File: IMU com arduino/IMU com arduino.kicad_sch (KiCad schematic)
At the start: 2 parts

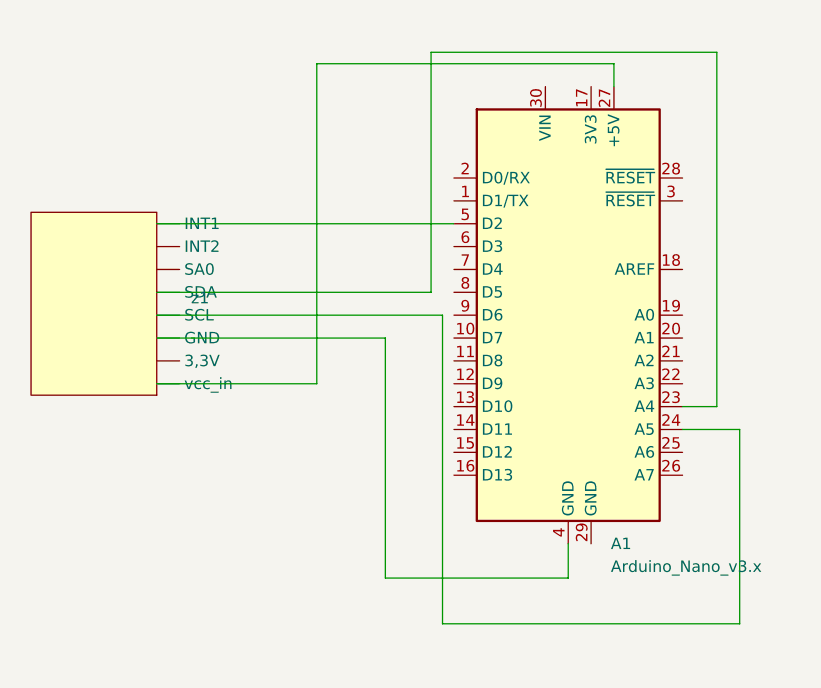
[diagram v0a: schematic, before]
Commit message: placa da imu com arduino para teste
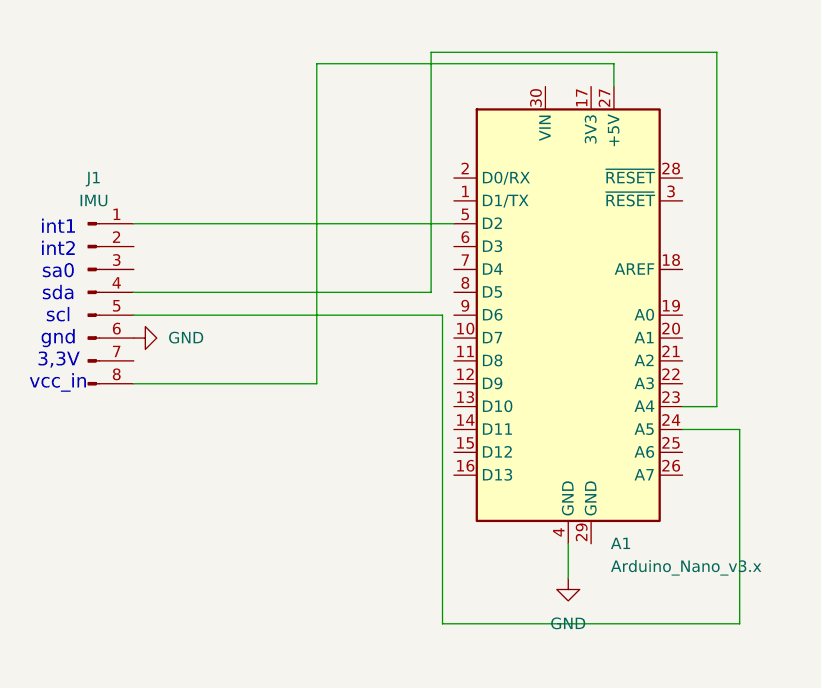
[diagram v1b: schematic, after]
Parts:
- removed z1: ~, symbol mm845x bib:mm845x
- added J1: IMU, Connector_PinSocket_2.54mm:PinSocket_1x08_P2.54mm_Vertical, symbol Connector:Conn_01x08_Pin
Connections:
- net at A1.23 (A4): now also J1.4 (Pin_4)
- net at A1.24 (A5): now also J1.5 (Pin_5)
- net at A1.27 (+5V): now also J1.8 (Pin_8)
- net GND: now reaches A1.4 (GND)
- net GND: now also J1.6 (Pin_6)
- net at A1.5 (D2): now also J1.1 (Pin_1)
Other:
- note added: "int1 int2 sa0 sda scl gnd 3,3V vcc_in"
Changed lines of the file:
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@@
-	(wire
-		(pts
-			(xy 87.63 57.15) (xy 87.63 83.82)
-		)
-		(stroke
-			(width 0)
-			(type default)
-		)
-	)
-	(wire
-		(pts
-			(xy 62.23 44.45) (xy 95.25 44.45)
-		)
-		(stroke
-			(width 0)
-			(type default)
-		)
-	)
 	(wire
 		(pts
@@
 	(wire
 		(pts
-			(xy 87.63 83.82) (xy 107.95 83.82)
-		)
-		(stroke
-			(width 0)
-			(type default)
-		)
-	)
-	(wire
-		(pts
-			(xy 62.23 57.15) (xy 87.63 57.15)
-		)
-		(stroke
-			(width 0)
-			(type default)
-		)
-	)
-	(wire
-		(pts
 			(xy 80.01 26.67) (xy 113.03 26.67)
 		)
@@
 	(wire
 		(pts
-			(xy 62.23 52.07) (xy 92.71 52.07)
+			(xy 59.69 52.07) (xy 92.71 52.07)
 		)
 		(stroke
@@
 	(wire
 		(pts
-			(xy 62.23 62.23) (xy 80.01 62.23)
-		)
-		(stroke
-			(width 0)
-			(type default)
-		)
-	)
-	(wire
-		(pts
-			(xy 62.23 54.61) (xy 93.98 54.61)
+			(xy 59.69 54.61) (xy 93.98 54.61)
+		)
+		(stroke
+			(width 0)
+			(type default)
+		)
+	)
+	(wire
+		(pts
+			(xy 59.69 62.23) (xy 80.01 62.23)
 		)
 		(stroke
@@
 	(wire
 		(pts
+			(xy 59.69 44.45) (xy 95.25 44.45)
+		)
+		(stroke
+			(width 0)
+			(type default)
+		)
+	)
+	(wire
+		(pts
 			(xy 93.98 88.9) (xy 127 88.9)
 		)
@@
 			(width 0)
 			(type default)
+		)
+	)
+	(text "int1\nint2\nsa0\nsda\nscl\ngnd\n3,3V\nvcc_in"
+		(exclude_from_sim no)
+		(at 51.308 53.594 0)
+		(effects
+			(font
+				(size 1.524 1.524)
+			)
 		)
 	)
@@
 	)
 	(symbol
-		(lib_id "mm845x bib:mm845x")
-		(at 46.99 55.88 180)
+		(lib_id "Connector:Conn_01x08_Pin")
+		(at 54.61 52.07 0)
 		(unit 1)
 		(exclude_from_sim no)
@@
 		(dnp no)
 		(fields_autoplaced yes)
-		(property "Reference" "z1"
-			(at 66.04 52.7049 0)
-			(effects
-				(font
-					(size 1.27 1.27)
-				)
-				(justify right)
-			)
-		)
-		(property "Value" "~"
-			(at 66.04 54.61 0)
-			(effects
-				(font
-					(size 1.27 1.27)
-				)
-				(justify right)
-			)
-		)
-		(property "Footprint" ""
-			(at 46.99 55.88 0)
-			(effects
-				(font
-					(size 1.27 1.27)
-				)
-				(hide yes)
-			)
-		)
-		(property "Datasheet" ""
-			(at 46.99 55.88 0)
-			(effects
-				(font
-					(size 1.27 1.27)
-				)
-				(hide yes)
-			)
-		)
-		(property "Description" ""
-			(at 46.99 55.88 0)
-			(effects
-				(font
-					(size 1.27 1.27)
-				)
-				(hide yes)
-			)
-		)
-		(pin ""
-		)
-		(pin ""
-		)
-		(pin ""
-		)
-		(pin ""
-		)
-		(pin ""
-		)
-		(pin ""
-		)
-		(pin ""
-		)
-		(pin ""
+		(property "Reference" "J1"
+			(at 55.245 39.37 0)
+			(effects
+				(font
+					(size 1.27 1.27)
+				)
+			)
+		)
+		(property "Value" "IMU"
+			(at 55.245 41.91 0)
+			(effects
+				(font
+					(size 1.27 1.27)
+				)
+			)
+		)
+		(property "Footprint" "Connector_PinSocket_2.54mm:PinSocket_1x08_P2.54mm_Vertical"
+			(at 54.61 52.07 0)
+			(effects
+				(font
+					(size 1.27 1.27)
+				)
+				(hide yes)
+			)
+		)
+		(property "Datasheet" "~"
+			(at 54.61 52.07 0)
+			(effects
+				(font
+					(size 1.27 1.27)
+				)
+				(hide yes)
+			)
+		)
+		(property "Description" "Generic connector, single row, 01x08, script generated"
+			(at 54.61 52.07 0)
+			(effects
+				(font
+					(size 1.27 1.27)
+				)
+				(hide yes)
+			)
+		)
+		(pin "6"
+		)
+		(pin "1"
+		)
+		(pin "7"
+		)
+		(pin "3"
+		)
+		(pin "8"
+		)
+		(pin "5"
+		)
+		(pin "2"
+		)
+		(pin "4"
 		)
 		(instances
 			(project ""
 				(path "/c62b45d3-c8bc-4f69-a5f4-d5875c176c61"
-					(reference "z1")
+					(reference "J1")
 					(unit 1)
 				)
+			)
+		)
+	)
+	(symbol
+		(lib_id "power:GND")
+		(at 107.95 83.82 0)
+		(unit 1)
+		(exclude_from_sim no)
+		(in_bom yes)
+		(on_board yes)
+		(dnp no)
+		(fields_autoplaced yes)
+		(property "Reference" "#PWR02"
+			(at 107.95 90.17 0)
+			(effects
+				(font
+					(size 1.27 1.27)
+				)
+				(hide yes)
+			)
+		)
+		(property "Value" "GND"
+			(at 107.95 88.9 0)
+			(effects
+				(font
+					(size 1.27 1.27)
+				)
+			)
+		)
+		(property "Footprint" ""
+			(at 107.95 83.82 0)
+			(effects
+				(font
+					(size 1.27 1.27)
+				)
+				(hide yes)
+			)
+		)
+		(property "Datasheet" ""
+			(at 107.95 83.82 0)
+			(effects
+				(font
+					(size 1.27 1.27)
+				)
+				(hide yes)
+			)
+		)
+		(property "Description" "Power symbol creates a global label with name \"GND\" , ground"
+			(at 107.95 83.82 0)
+			(effects
+				(font
+					(size 1.27 1.27)
+				)
+				(hide yes)
+			)
+		)
+		(pin "1"
+		)
+		(instances
+			(project "IMU com arduino"
+				(path "/c62b45d3-c8bc-4f69-a5f4-d5875c176c61"
+					(reference "#PWR02")
+					(unit 1)
+				)
+			)
+		)
+	)
+	(symbol
+		(lib_id "power:GND")
+		(at 59.69 57.15 90)
+		(unit 1)
+		(exclude_from_sim no)
+		(in_bom yes)
+		(on_board yes)
+		(dnp no)
+		(fields_autoplaced yes)
+		(property "Reference" "#PWR01"
+			(at 66.04 57.15 0)
+			(effects
+				(font
+					(size 1.27 1.27)
+				)
+				(hide yes)
+			)
+		)
+		(property "Value" "GND"
+			(at 63.5 57.1499 90)
+			(effects
+				(font
+					(size 1.27 1.27)
+				)
+				(justify right)
+			)
+		)
+		(property "Footprint" ""
+			(at 59.69 57.15 0)
+			(effects
+				(font
+					(size 1.27 1.27)
+				)
+				(hide yes)
+			)
+		)
+		(property "Datasheet" ""
+			(at 59.69 57.15 0)
+			(effects
+				(font
+					(size 1.27 1.27)
+				)
+				(hide yes)
+			)
+		)
+		(property "Description" "Power symbol creates a global label with name \"GND\" , ground"
+			(at 59.69 57.15 0)
+			(effects
+				(font
+					(size 1.27 1.27)
+				)
+				(hide yes)
+			)
+		)
+		(pin "1"
+		)
+		(instances
+			(project ""
+				(path "/c62b45d3-c8bc-4f69-a5f4-d5875c176c61"
+					(reference "#PWR01")
+					(unit 1)
+				)

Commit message: imu nova (MPU6050)
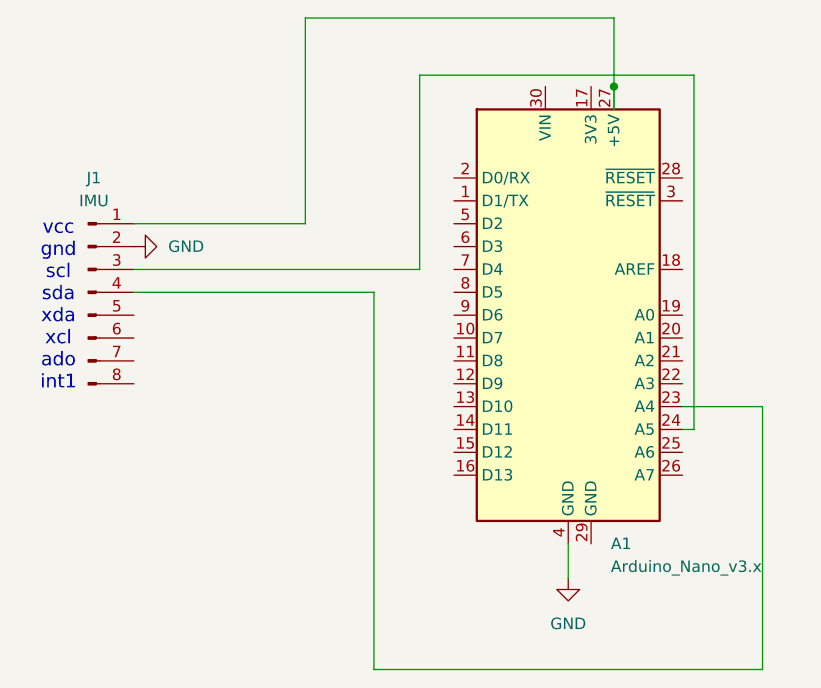
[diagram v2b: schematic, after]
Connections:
- net GND: now also J1.2 (Pin_2); no longer J1.6 (Pin_6)
- net at A1.24 (A5): now also J1.3 (Pin_3); no longer J1.5 (Pin_5)
- net at A1.27 (+5V): now also J1.1 (Pin_1); no longer J1.8 (Pin_8)
- net at A1.5 (D2): no longer J1.1 (Pin_1)
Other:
- note added: "vcc gnd scl sda xda xcl ado int1"
- note removed: "int1 int2 sa0 sda scl gnd 3,3V vcc_in"
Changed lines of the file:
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@@
 	(generator_version "8.0")
 	(paper "A4")
-	(wire
-		(pts
-			(xy 93.98 54.61) (xy 93.98 88.9)
-		)
-		(stroke
-			(width 0)
-			(type default)
-		)
-	)
-	(wire
-		(pts
-			(xy 124.46 64.77) (xy 120.65 64.77)
-		)
-		(stroke
-			(width 0)
-			(type default)
-		)
-	)
-	(wire
-		(pts
-			(xy 80.01 26.67) (xy 113.03 26.67)
-		)
-		(stroke
-			(width 0)
-			(type default)
-		)
-	)
-	(wire
-		(pts
-			(xy 124.46 25.4) (xy 124.46 64.77)
-		)
-		(stroke
-			(width 0)
-			(type default)
-		)
-	)
-	(wire
-		(pts
-			(xy 59.69 52.07) (xy 92.71 52.07)
-		)
-		(stroke
-			(width 0)
-			(type default)
-		)
-	)
-	(wire
-		(pts
-			(xy 92.71 52.07) (xy 92.71 25.4)
-		)
-		(stroke
-			(width 0)
-			(type default)
-		)
-	)
-	(wire
-		(pts
-			(xy 113.03 26.67) (xy 113.03 29.21)
-		)
-		(stroke
-			(width 0)
-			(type default)
-		)
-	)
-	(wire
-		(pts
-			(xy 127 88.9) (xy 127 67.31)
-		)
-		(stroke
-			(width 0)
-			(type default)
-		)
-	)
-	(wire
-		(pts
-			(xy 92.71 25.4) (xy 124.46 25.4)
-		)
-		(stroke
-			(width 0)
-			(type default)
-		)
-	)
-	(wire
-		(pts
-			(xy 127 67.31) (xy 120.65 67.31)
-		)
-		(stroke
-			(width 0)
-			(type default)
-		)
-	)
-	(wire
-		(pts
-			(xy 59.69 54.61) (xy 93.98 54.61)
-		)
-		(stroke
-			(width 0)
-			(type default)
-		)
-	)
-	(wire
-		(pts
-			(xy 59.69 62.23) (xy 80.01 62.23)
-		)
-		(stroke
-			(width 0)
-			(type default)
-		)
-	)
-	(wire
-		(pts
-			(xy 80.01 62.23) (xy 80.01 26.67)
+	(junction
+		(at 113.03 29.21)
+		(diameter 0)
+		(color 0 0 0 0)
+	)
+	(wire
+		(pts
+			(xy 91.44 49.53) (xy 91.44 27.94)
+		)
+		(stroke
+			(width 0)
+			(type default)
+		)
+	)
+	(wire
+		(pts
+			(xy 86.36 93.98) (xy 129.54 93.98)
+		)
+		(stroke
+			(width 0)
+			(type default)
+		)
+	)
+	(wire
+		(pts
+			(xy 59.69 49.53) (xy 91.44 49.53)
+		)
+		(stroke
+			(width 0)
+			(type default)
+		)
+	)
+	(wire
+		(pts
+			(xy 121.92 67.31) (xy 120.65 67.31)
+		)
+		(stroke
+			(width 0)
+			(type default)
+		)
+	)
+	(wire
+		(pts
+			(xy 121.92 27.94) (xy 121.92 67.31)
+		)
+		(stroke
+			(width 0)
+			(type default)
+		)
+	)
+	(wire
+		(pts
+			(xy 129.54 64.77) (xy 129.54 93.98)
+		)
+		(stroke
+			(width 0)
+			(type default)
+		)
+	)
+	(wire
+		(pts
+			(xy 59.69 52.07) (xy 86.36 52.07)
+		)
+		(stroke
+			(width 0)
+			(type default)
+		)
+	)
+	(wire
+		(pts
+			(xy 113.03 21.59) (xy 113.03 29.21)
+		)
+		(stroke
+			(width 0)
+			(type default)
+		)
+	)
+	(wire
+		(pts
+			(xy 78.74 44.45) (xy 78.74 21.59)
+		)
+		(stroke
+			(width 0)
+			(type default)
+		)
+	)
+	(wire
+		(pts
+			(xy 91.44 27.94) (xy 121.92 27.94)
 		)
 		(stroke
@@
 	(wire
 		(pts
-			(xy 59.69 44.45) (xy 95.25 44.45)
-		)
-		(stroke
-			(width 0)
-			(type default)
-		)
-	)
-	(wire
-		(pts
-			(xy 93.98 88.9) (xy 127 88.9)
-		)
-		(stroke
-			(width 0)
-			(type default)
-		)
-	)
-	(text "int1\nint2\nsa0\nsda\nscl\ngnd\n3,3V\nvcc_in"
+			(xy 59.69 44.45) (xy 78.74 44.45)
+		)
+		(stroke
+			(width 0)
+			(type default)
+		)
+	)
+	(wire
+		(pts
+			(xy 129.54 64.77) (xy 120.65 64.77)
+		)
+		(stroke
+			(width 0)
+			(type default)
+		)
+	)
+	(wire
+		(pts
+			(xy 78.74 21.59) (xy 113.03 21.59)
+		)
+		(stroke
+			(width 0)
+			(type default)
+		)
+	)
+	(wire
+		(pts
+			(xy 113.03 29.21) (xy 113.03 31.75)
+		)
+		(stroke
+			(width 0)
+			(type default)
+		)
+	)
+	(wire
+		(pts
+			(xy 86.36 52.07) (xy 86.36 93.98)
+		)
+		(stroke
+			(width 0)
+			(type default)
+		)
+	)
+	(text "vcc\ngnd\nscl\nsda\nxda\nxcl\nado\nint1"
 		(exclude_from_sim no)
 		(at 51.308 53.594 0)
@@
 	(symbol
 		(lib_id "power:GND")
-		(at 59.69 57.15 90)
+		(at 59.69 46.99 90)
 		(unit 1)
 		(exclude_from_sim no)
@@
 		(fields_autoplaced yes)
 		(property "Reference" "#PWR01"
-			(at 66.04 57.15 0)
+			(at 66.04 46.99 0)
 			(effects
 				(font
@@
 		)
 		(property "Value" "GND"
-			(at 63.5 57.1499 90)
+			(at 63.5 46.9899 90)
 			(effects
 				(font
@@
 		)
 		(property "Footprint" ""
-			(at 59.69 57.15 0)
+			(at 59.69 46.99 0)
 			(effects
 				(font
@@
 		)
 		(property "Datasheet" ""
-			(at 59.69 57.15 0)
+			(at 59.69 46.99 0)
 			(effects
 				(font
@@
 		)
 		(property "Description" "Power symbol creates a global label with name \"GND\" , ground"
-			(at 59.69 57.15 0)
-			(effects
-				(font
+			(at 59.69 46.99 0)
+			(effects
+				(font
